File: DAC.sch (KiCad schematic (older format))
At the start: 21 parts, among them U2 PCM5102, U3 AP1117-33

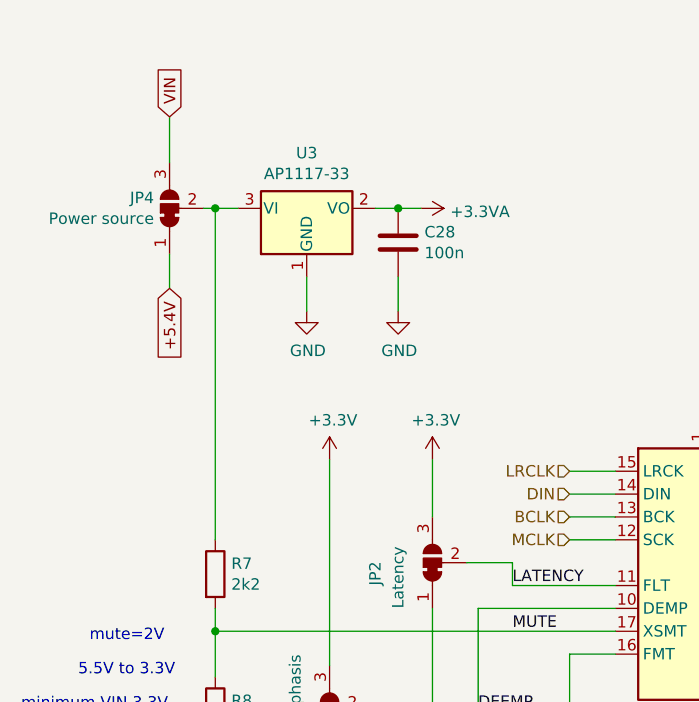
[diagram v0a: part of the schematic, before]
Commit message: solder paste at 90%; changed LDO
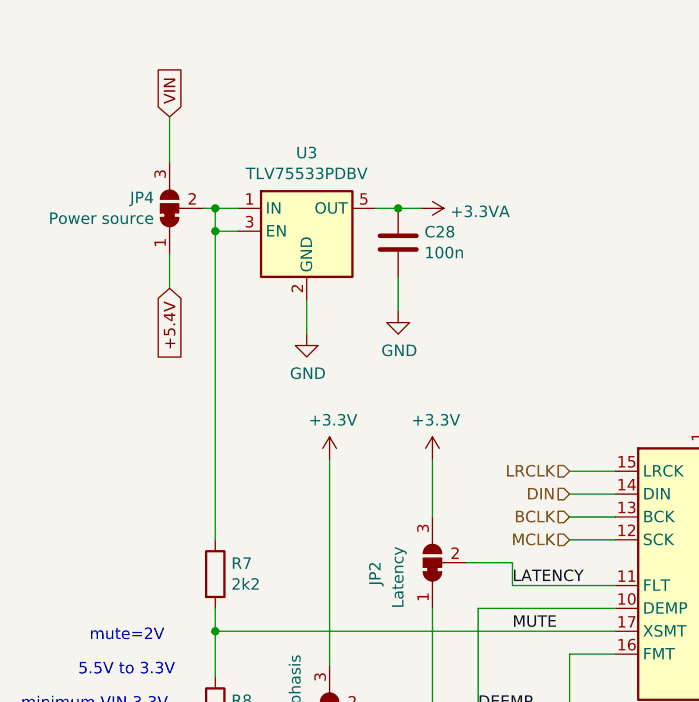
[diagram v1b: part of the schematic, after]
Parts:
- removed U3: AP1117-33, Package_TO_SOT_SMD:SOT-223-3_TabPin2, symbol Regulator_Linear:AP1117-33
- added U3: TLV75533PDBV, Package_TO_SOT_SMD:SOT-23-5, symbol Regulator_Linear:TLV75533PDBV
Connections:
- net +3.3VA: now also U3.5 (OUT)
- net GND: now also U3.2 (GND)
- net at JP4.2 (C), R7.1: now also U3.1 (IN), U3.3 (EN)
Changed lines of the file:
@@
 L power:GND #PWR047
 U 1 1 5D457C9B
-P 3600 2600
-F 0 "#PWR047" H 3600 2350 50  0001 C CNN
-F 1 "GND" H 3605 2427 50  0000 C CNN
-F 2 "" H 3600 2600 50  0001 C CNN
-F 3 "" H 3600 2600 50  0001 C CNN
-	1    3600 2600
+P 3600 2700
+F 0 "#PWR047" H 3600 2450 50  0001 C CNN
+F 1 "GND" H 3605 2527 50  0000 C CNN
+F 2 "" H 3600 2700 50  0001 C CNN
+F 3 "" H 3600 2700 50  0001 C CNN
+	1    3600 2700
 	1    0    0    -1
 $EndComp
@@
 $EndComp
 Wire Wire Line
-	3600 2450 3600 2600
+	3600 2550 3600 2700
 Wire Wire Line
 	3900 2150 4000 2150
@@
 	3000 2500 3000 2350
 Wire Wire Line
-	3200 3600 3200 2150
+	3200 3600 3200 2250
 Connection ~ 3200 2150
 Wire Wire Line
@@
 	4150 3250 4150 3500
 $Comp
-L Regulator_Linear:AP1117-33 U3
-U 1 1 5D456577
-P 3600 2150
-F 0 "U3" H 3600 2392 50  0000 C CNN
-F 1 "AP1117-33" H 3600 2301 50  0000 C CNN
-F 2 "Package_TO_SOT_SMD:SOT-223-3_TabPin2" H 3600 2350 50  0001 C CNN
-F 3 "http://www.diodes.com/datasheets/AP1117.pdf" H 3700 1900 50  0001 C CNN
-	1    3600 2150
+L Regulator_Linear:TLV75533PDBV U3
+U 1 1 5E0A56B0
+P 3600 2250
+F 0 "U3" H 3600 2592 50  0000 C CNN
+F 1 "TLV75533PDBV" H 3600 2501 50  0000 C CNN
+F 2 "Package_TO_SOT_SMD:SOT-23-5" H 3600 2550 50  0001 C CIN
+F 3 "http://www.ti.com/lit/ds/symlink/tlv755p.pdf" H 3600 2250 50  0001 C CNN
+	1    3600 2250
 	1    0    0    -1
 $EndComp
+Wire Wire Line
+	3300 2250 3200 2250
+Connection ~ 3200 2250
+Wire Wire Line
+	3200 2250 3200 2150
 $EndSCHEMATC
